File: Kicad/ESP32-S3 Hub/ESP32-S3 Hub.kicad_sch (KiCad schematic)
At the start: 26 parts, among them U1 ESP32-S3, Y1 ABM11-40.000MHZ-B1U-T3, 10ppm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

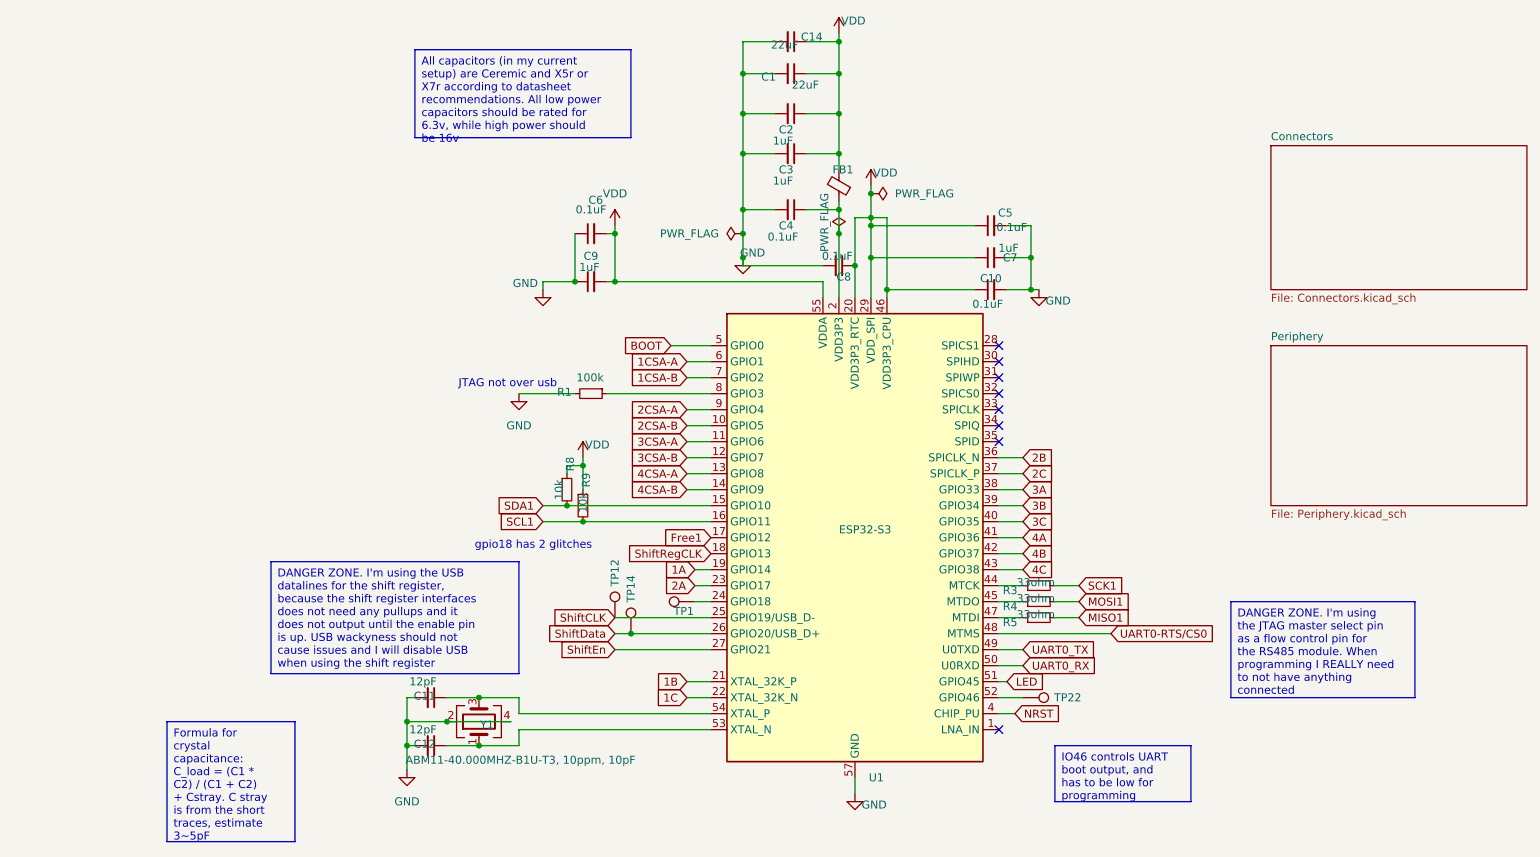
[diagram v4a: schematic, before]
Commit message: Swapping register pins
I tryid to simplify the layout a little bit. I also added a note about the potential danger of the i2c lines on low level glitching pins.
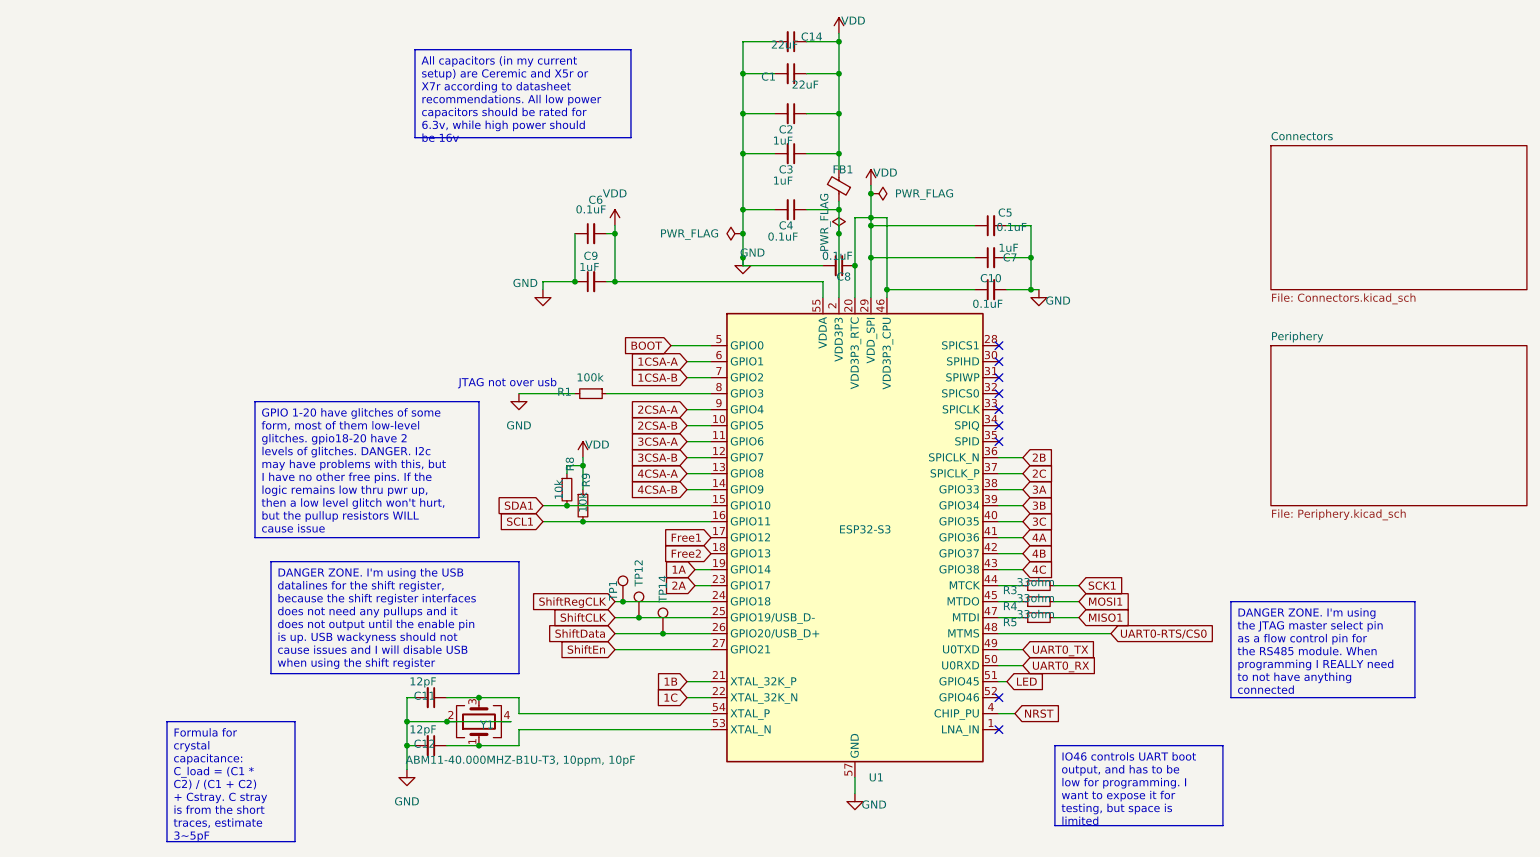
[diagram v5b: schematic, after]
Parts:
- removed TP22: ~, TestPoint:TestPoint_Pad_D1.0mm, symbol Connector:TestPoint
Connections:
- net ShiftRegCLK: now also TP1.1, U1.24 (GPIO18); no longer U1.18 (GPIO13)
- new net Free2: U1.18 (GPIO13)
- no-connect marks 8 -> 9
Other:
- note removed: "gpio18 has 2 glitches"
- moved on the sheet: TP1, TP12, TP14
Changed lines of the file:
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@@
 	)
 	(junction
+		(at 110.49 105.41)
+		(diameter 0)
+		(color 0 0 0 0)
+	)
+	(junction
+		(at 107.95 102.87)
+		(diameter 0)
+		(color 0 0 0 0)
+	)
+	(junction
 		(at 127 48.26)
 		(diameter 0)
@@
 	)
 	(junction
-		(at 109.22 107.95)
+		(at 142.24 19.05)
 		(diameter 0)
 		(color 0 0 0 0)
 	)
 	(junction
-		(at 142.24 19.05)
+		(at 127 44.45)
 		(diameter 0)
 		(color 0 0 0 0)
 	)
 	(junction
-		(at 127 44.45)
+		(at 73.66 121.92)
 		(diameter 0)
 		(color 0 0 0 0)
 	)
 	(junction
-		(at 73.66 121.92)
+		(at 114.3 107.95)
 		(diameter 0)
 		(color 0 0 0 0)
@@
 	)
 	(no_connect
+		(at 167.64 118.11)
+	)
+	(no_connect
 		(at 167.64 64.77)
 	)
@@
 	(wire
 		(pts
-			(xy 119.38 102.87) (xy 121.92 102.87)
+			(xy 167.64 105.41) (xy 171.45 105.41)
 		)
 		(stroke
@@
 	(wire
 		(pts
-			(xy 167.64 105.41) (xy 171.45 105.41)
+			(xy 107.95 102.87) (xy 121.92 102.87)
 		)
 		(stroke
@@
 	(wire
 		(pts
-			(xy 109.22 107.95) (xy 121.92 107.95)
-		)
-		(stroke
-			(width 0)
-			(type default)
-		)
-	)
-	(wire
-		(pts
 			(xy 119.38 100.33) (xy 121.92 100.33)
 		)
@@
 	(wire
 		(pts
+			(xy 106.68 102.87) (xy 107.95 102.87)
+		)
+		(stroke
+			(width 0)
+			(type default)
+		)
+	)
+	(wire
+		(pts
 			(xy 101.6 90.17) (xy 121.92 90.17)
 		)
@@
 	(wire
 		(pts
+			(xy 110.49 105.41) (xy 121.92 105.41)
+		)
+		(stroke
+			(width 0)
+			(type default)
+		)
+	)
+	(wire
+		(pts
 			(xy 139.7 54.61) (xy 139.7 52.07)
 		)
@@
 	(wire
 		(pts
-			(xy 106.68 107.95) (xy 109.22 107.95)
+			(xy 106.68 107.95) (xy 114.3 107.95)
 		)
 		(stroke
@@
 	(wire
 		(pts
-			(xy 171.45 118.11) (xy 167.64 118.11)
-		)
-		(stroke
-			(width 0)
-			(type default)
-		)
-	)
-	(wire
-		(pts
 			(xy 118.11 74.93) (xy 121.92 74.93)
 		)
@@
 	(wire
 		(pts
-			(xy 106.68 105.41) (xy 121.92 105.41)
+			(xy 114.3 107.95) (xy 121.92 107.95)
+		)
+		(stroke
+			(width 0)
+			(type default)
+		)
+	)
+	(wire
+		(pts
+			(xy 106.68 105.41) (xy 110.49 105.41)
 		)
 		(stroke
@@
 		)
 	)
-	(text_box "IO46 controls UART boot output, and has to be low for programming"
+	(text_box "IO46 controls UART boot output, and has to be low for programming. I want to expose it for testing, but space is limited"
 		(exclude_from_sim no)
 		(at 176.53 125.73 0)
-		(size 21.59 8.89)
+		(size 26.67 12.7)
 		(stroke
 			(width 0)
@@
 		)
 	)
-	(text_box "Formula for crystal capacitance: C_load = (C1 * C2) / (C1 + C2) + Cstray. C stray is from the short traces, estimate 3~5pF"
+	(text_box "GPIO 1-20 have glitches of some form, most of them low-level glitches. gpio18-20 have 2 levels of glitches. DANGER. I2c may have problems with this, but I have no other free pins. If the logic remains low thru pwr up, then a low level glitch won't hurt, but the pullup resistors WILL cause issue"
 		(exclude_from_sim no)
-		(at 35.56 121.92 0)
-		(size 20.32 19.05)
+		(at 49.53 71.12 0)
+		(size 35.56 21.59)
 		(stroke
 			(width 0)
@@
 		)
 	)
-	(text "JTAG not over usb"
+	(text_box "Formula for crystal capacitance: C_load = (C1 * C2) / (C1 + C2) + Cstray. C stray is from the short traces, estimate 3~5pF"
 		(exclude_from_sim no)
-		(at 89.662 68.326 0)
+		(at 35.56 121.92 0)
+		(size 20.32 19.05)
+		(stroke
+			(width 0)
+			(type default)
+		)
+		(fill
+			(type none)
+		)
 		(effects
 			(font
 				(size 1.27 1.27)
 			)
+			(justify left top)
 		)
 	)
-	(text "gpio18 has 2 glitches"
+	(text "JTAG not over usb"
 		(exclude_from_sim no)
-		(at 93.726 93.98 0)
+		(at 89.662 68.326 0)
 		(effects
 			(font
@@
 		)
 	)
+	(global_label "Free2"
+		(shape input)
+		(at 121.92 95.25 180)
+		(fields_autoplaced yes)
+		(effects
+			(font
+				(size 1.27 1.27)
+			)
+			(justify right)
+		)
+		(property "Intersheetrefs" "${INTERSHEET_REFS}"
+			(at 113.6733 95.25 0)
+			(effects
+				(font
+					(size 1.27 1.27)
+				)
+				(justify right)
+				(hide yes)
+			)
+		)
+	)
 	(global_label "UART0_RX"
 		(shape input)
@@
 	(global_label "ShiftRegCLK"
 		(shape input)
-		(at 121.92 95.25 180)
+		(at 106.68 102.87 180)
 		(fields_autoplaced yes)
 		(effects
@@
 		)
 		(property "Intersheetrefs" "${INTERSHEET_REFS}"
-			(at 107.4444 95.25 0)
+			(at 92.2044 102.87 0)
 			(effects
 				(font
@@
 	(symbol
 		(lib_id "Connector:TestPoint")
-		(at 119.38 102.87 90)
+		(at 107.95 102.87 0)
 		(unit 1)
 		(exclude_from_sim no)
@@
 		(dnp no)
 		(property "Reference" "TP1"
-			(at 117.602 104.394 90)
+			(at 106.426 101.092 90)
 			(effects
 				(font
@@
 		)
 		(property "Value" "~"
-			(at 110.49 102.616 90)
+			(at 108.204 93.98 90)
 			(effects
 				(font
@@
 		)
 		(property "Footprint" "TestPoint:TestPoint_Pad_D1.0mm"
-			(at 119.38 97.79 0)
+			(at 113.03 102.87 0)
 			(effects
 				(font
@@
 		)
 		(property "Datasheet" "~"
-			(at 119.38 97.79 0)
+			(at 113.03 102.87 0)
 			(effects
 				(font
@@
 		)
 		(property "Description" "test point"
-			(at 119.38 102.87 0)
+			(at 107.95 102.87 0)
 			(effects
 				(font
@@
 	(symbol
 		(lib_id "Connector:TestPoint")
-		(at 109.22 107.95 0)
+		(at 114.3 107.95 0)
 		(unit 1)
 		(exclude_from_sim no)
@@
 		(dnp no)
 		(property "Reference" "TP14"
-			(at 109.22 100.838 90)
+			(at 114.3 100.838 90)
 			(effects
 				(font
@@
 		)
 		(property "Value" "~"
-			(at 109.474 99.06 90)
+			(at 114.554 99.06 90)
 			(effects
 				(font
@@
 		)
 		(property "Footprint" "TestPoint:TestPoint_Pad_D1.0mm"
-			(at 114.3 107.95 0)
+			(at 119.38 107.95 0)
 			(effects
 				(font
@@
 		)
 		(property "Datasheet" "~"
-			(at 114.3 107.95 0)
+			(at 119.38 107.95 0)
 			(effects
 				(font
@@
 		)
 		(property "Description" "test point"
-			(at 109.22 107.95 0)
+			(at 114.3 107.95 0)
 			(effects
 				(font
@@
 	(symbol
 		(lib_id "Connector:TestPoint")
-		(at 106.68 105.41 0)
+		(at 110.49 105.41 0)
 		(unit 1)
 		(exclude_from_sim no)
@@
 		(dnp no)
 		(property "Reference" "TP12"
-			(at 106.68 98.298 90)
+			(at 110.49 98.298 90)
 			(effects
 				(font
@@
 		)
 		(property "Value" "~"
-			(at 106.934 96.52 90)
+			(at 110.744 96.52 90)
 			(effects
 				(font
@@
 		)
 		(property "Footprint" "TestPoint:TestPoint_Pad_D1.0mm"
-			(at 111.76 105.41 0)
+			(at 115.57 105.41 0)
 			(effects
 				(font
@@
 		)
 		(property "Datasheet" "~"
-			(at 111.76 105.41 0)
+			(at 115.57 105.41 0)
 			(effects
 				(font
@@
 		)
 		(property "Description" "test point"
-			(at 106.68 105.41 0)
+			(at 110.49 105.41 0)
 			(effects
 				(font
@@
 					(unit 1)
 				)
-			)
-		)
-	)
-	(symbol
-		(lib_id "Connector:TestPoint")
-		(at 171.45 118.11 270)
-		(unit 1)
-		(exclude_from_sim no)
-		(in_bom yes)
-		(on_board yes)
-		(dnp no)
-		(property "Reference" "TP22"
-			(at 178.562 118.11 90)
-			(effects
-				(font
-					(size 1.27 1.27)
-				)
-			)
-		)
-		(property "Value" "~"
-			(at 180.34 118.364 90)
-			(effects
-				(font
-					(size 1.27 1.27)
-				)
-			)
-		)
-		(property "Footprint" "TestPoint:TestPoint_Pad_D1.0mm"
-			(at 171.45 123.19 0)
-			(effects
-				(font
-					(size 1.27 1.27)
-				)
-				(hide yes)
-			)
-		)
-		(property "Datasheet" "~"
-			(at 171.45 123.19 0)
-			(effects
-				(font
-					(size 1.27 1.27)
-				)
-				(hide yes)
-			)
-		)
-		(property "Description" "test point"
-			(at 171.45 118.11 0)
-			(effects
-				(font
-					(size 1.27 1.27)
-				)
-				(hide yes)
-			)
-		)
-		(pin "1"
-		)
-		(instances
-			(project "ESP32-S3 Hub"
-				(path "/a8c80fba-3bca-4358-b5bb-9ebf9383c658"
-					(reference "TP22")
-					(unit 1)
-				)

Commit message: Fixed potential glitch problems caused by pullup resistors
I2c w/ pullups will likely have problems with glitching on those first 20 pins, so I have shifted all the motor pwm pins down, and stuck the FREEx pins and the i2c pins near the end. Now, only the motor pins and the analog pins will have glitching. Since it is a low level glitch, and there are no pullups on those lines, it should be fine.

I also added a note about a weird state on GPIO1
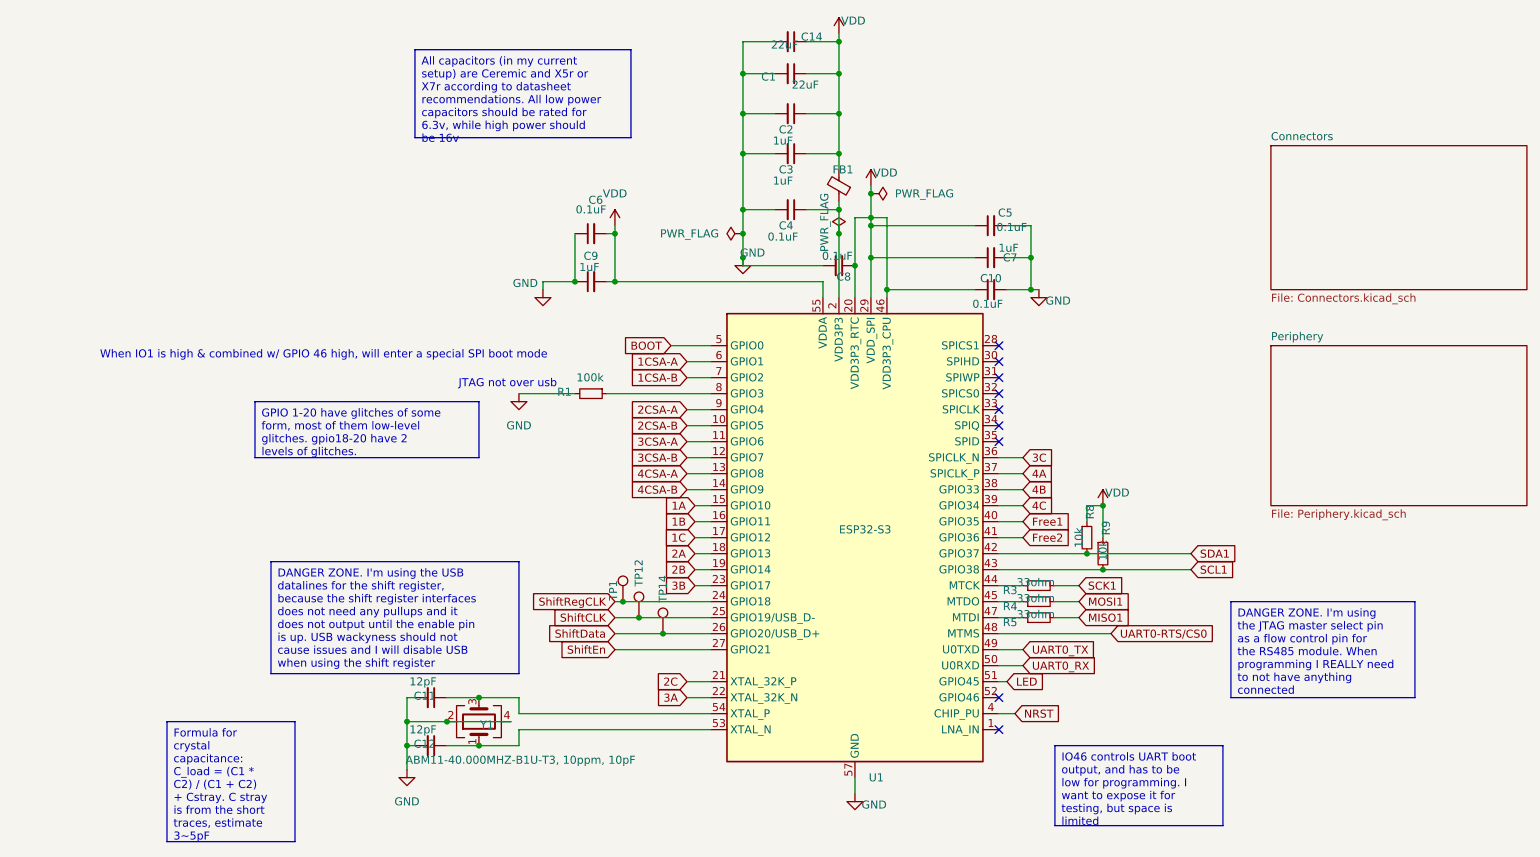
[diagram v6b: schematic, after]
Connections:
- net 1A: now also U1.15 (GPIO10); no longer U1.19 (GPIO14)
- net 1B: now also U1.16 (GPIO11); no longer U1.21 (XTAL_32K_P)
- net 1C: now also U1.17 (GPIO12); no longer U1.22 (XTAL_32K_N)
- net 2A: now also U1.18 (GPIO13); no longer U1.23 (GPIO17)
- net 2B: now also U1.19 (GPIO14); no longer U1.36 (SPICLK_N)
- net 2C: now also U1.21 (XTAL_32K_P); no longer U1.37 (SPICLK_P)
- net 3A: now also U1.22 (XTAL_32K_N); no longer U1.38 (GPIO33)
- net 3B: now also U1.23 (GPIO17); no longer U1.39 (GPIO34)
- net 3C: now also U1.36 (SPICLK_N); no longer U1.40 (GPIO35)
- net 4A: now also U1.37 (SPICLK_P); no longer U1.41 (GPIO36)
- net 4B: now also U1.38 (GPIO33); no longer U1.42 (GPIO37)
- net 4C: now also U1.39 (GPIO34); no longer U1.43 (GPIO38)
- net Free1: now also U1.40 (GPIO35); no longer U1.17 (GPIO12)
- net Free2: now also U1.41 (GPIO36); no longer U1.18 (GPIO13)
- net SCL1: now also U1.43 (GPIO38); no longer U1.16 (GPIO11)
- net SDA1: now also U1.42 (GPIO37); no longer U1.15 (GPIO10)
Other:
- note added: "When IO1 is high & combined w/ GPIO 46 high, will enter a special SPI boot mode"
- moved on the sheet: R8, R9

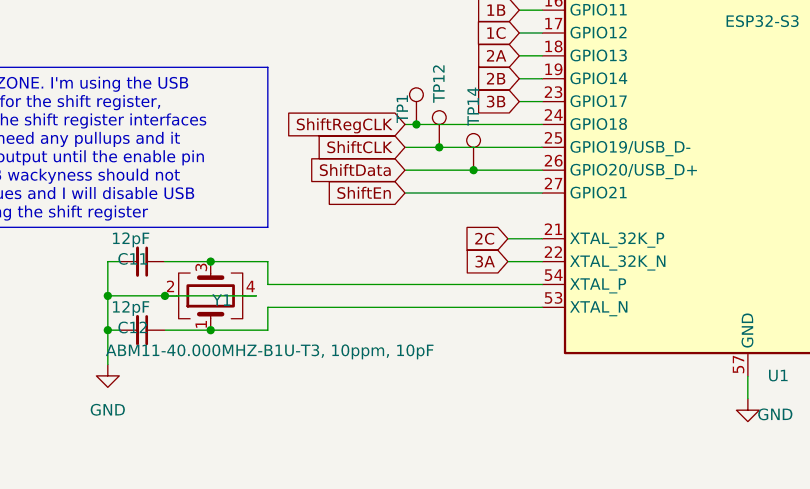
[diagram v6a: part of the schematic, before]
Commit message: Added ground keepouts and series resistor to crystal
The ground keepouts are mostly to prevent random areas of ground copper where I have limited space. The keepout was required for the crystal though.

I also added a 22 ohm series resistor to the crystal path, because many examples have that.
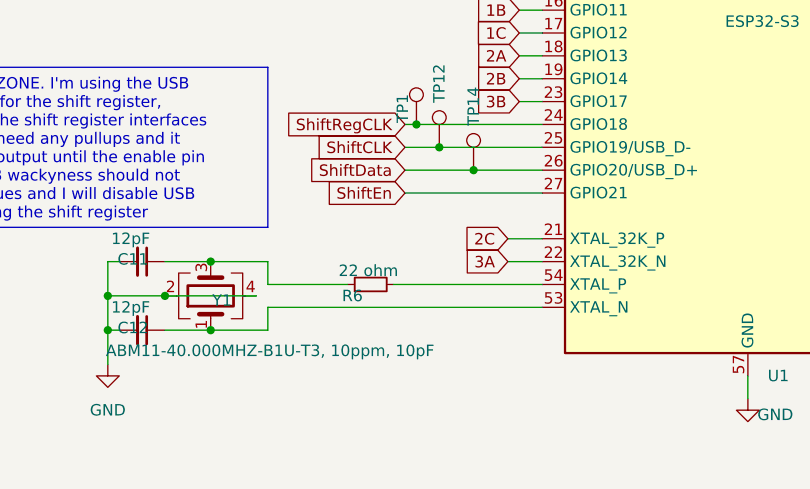
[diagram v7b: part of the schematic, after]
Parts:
- added R6: 22 ohm, Resistor_SMD:R_0402_1005Metric, symbol Device:R_Small
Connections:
- net at C11.1, Y1.3: now also R6.1; no longer U1.54 (XTAL_P)
- new net: R6.2, U1.54 (XTAL_P)
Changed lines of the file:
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@@
 	(wire
 		(pts
+			(xy 105.41 120.65) (xy 121.92 120.65)
+		)
+		(stroke
+			(width 0)
+			(type default)
+		)
+	)
+	(wire
+		(pts
 			(xy 167.64 105.41) (xy 171.45 105.41)
 		)
@@
 	(wire
 		(pts
-			(xy 91.44 120.65) (xy 121.92 120.65)
+			(xy 91.44 120.65) (xy 100.33 120.65)
 		)
 		(stroke
@@
 					(unit 1)
 				)
+			)
+		)
+	)
+	(symbol
+		(lib_id "Device:R_Small")
+		(at 102.87 120.65 90)
+		(unit 1)
+		(exclude_from_sim no)
+		(in_bom yes)
+		(on_board yes)
+		(dnp no)
+		(property "Reference" "R6"
+			(at 100.838 121.92 90)
+			(effects
+				(font
+					(size 1.27 1.27)
+				)
+			)
+		)
+		(property "Value" "22 ohm"
+			(at 102.616 119.126 90)
+			(effects
+				(font
+					(size 1.27 1.27)
+				)
+			)
+		)
+		(property "Footprint" "Resistor_SMD:R_0402_1005Metric"
+			(at 102.87 120.65 0)
+			(effects
+				(font
+					(size 1.27 1.27)
+				)
+				(hide yes)
+			)
+		)
+		(property "Datasheet" "~"
+			(at 102.87 120.65 0)
+			(effects
+				(font
+					(size 1.27 1.27)
+				)
+				(hide yes)
+			)
+		)
+		(property "Description" "Resistor, small symbol"
+			(at 102.87 120.65 0)
+			(effects
+				(font
+					(size 1.27 1.27)
+				)
+				(hide yes)
+			)
+		)
+		(pin "2"
+		)
+		(pin "1"
+		)
+		(instances
+			(project "ESP32-S3 Hub"
+				(path "/a8c80fba-3bca-4358-b5bb-9ebf9383c658"
+					(reference "R6")
+					(unit 1)
+				)
